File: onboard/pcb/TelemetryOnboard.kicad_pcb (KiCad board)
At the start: 4 copper layers, 95 x 95 mm, 143 parts, among them J1 USB-C, J2 USB-C, J3 RFPC-SMA28-F, J4 RFPC-SMA28-F, J5 Molex_MicroFit_2pin, M1 M4 Mounting Hole, M2 M4 Mounting Hole, M3 M4 Mounting Hole, M4 M4 Mounting Hole, Q1 MMBT4401-TP, U1 CP2102N, U2 CP2102N, U3 AVR128DB64x-xPT, U4 RC1780HP-RC232, U5 RC1701HP-RC232, U6 W25Q80DVSSIG

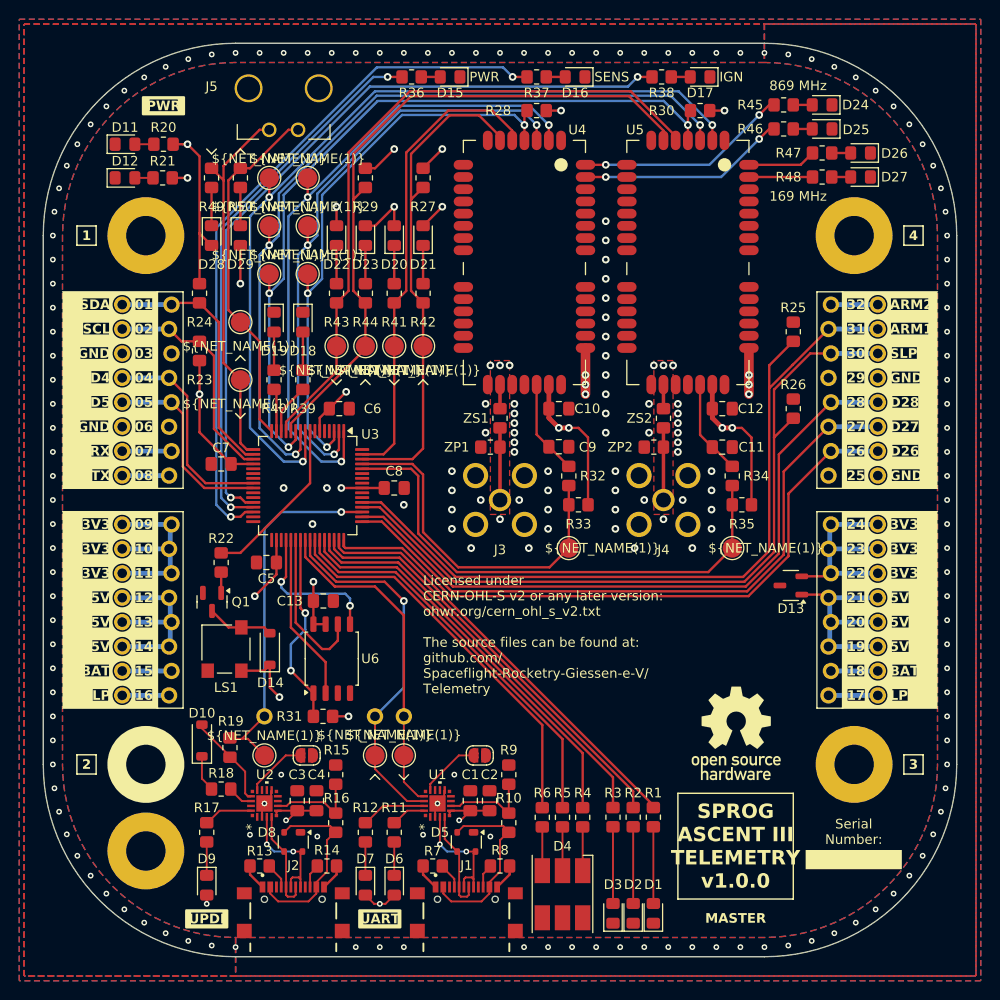
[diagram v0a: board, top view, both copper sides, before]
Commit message: delete unused onboard kicad 3d models
#82
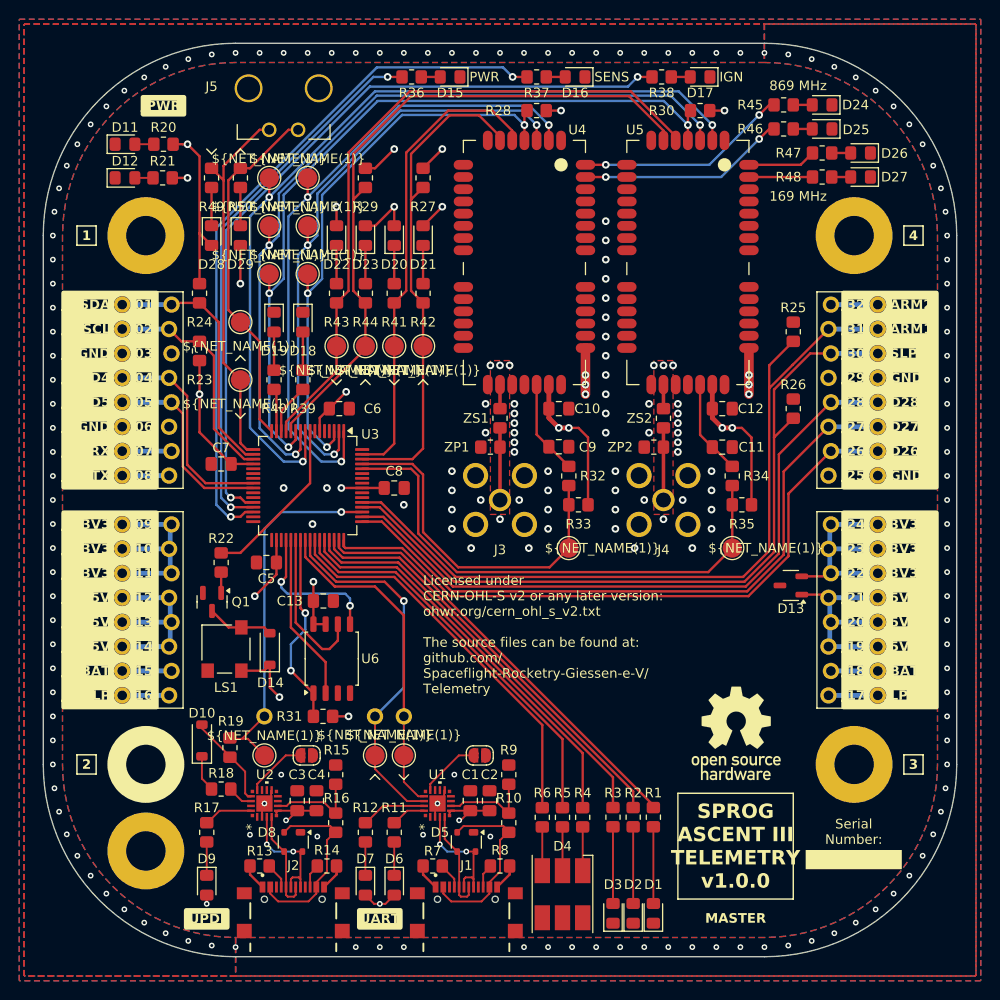
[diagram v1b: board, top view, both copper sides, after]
